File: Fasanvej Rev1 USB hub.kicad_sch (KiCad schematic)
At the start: 23 parts, among them U12 TUSB2036, U13 TPS2042D, Y2 6.000 MHz

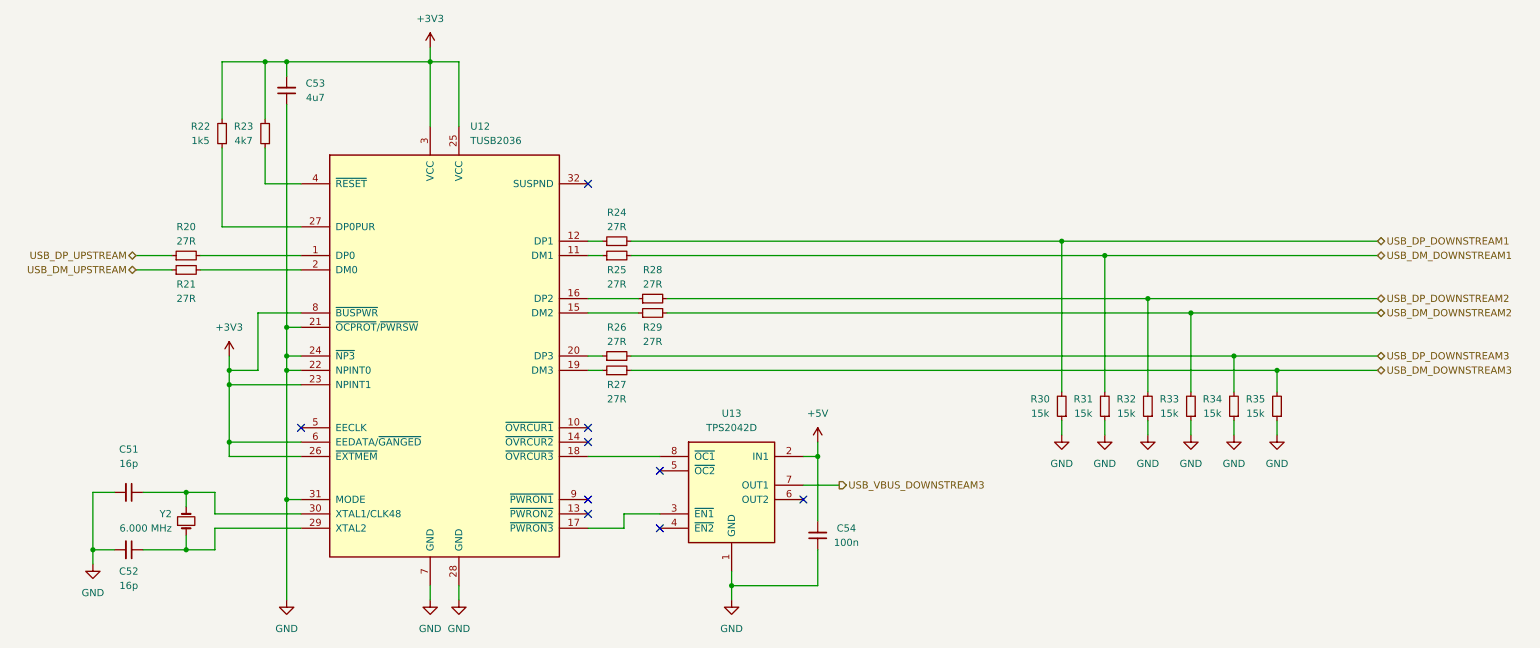
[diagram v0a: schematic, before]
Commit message: Made a lot of progress laying out PCB
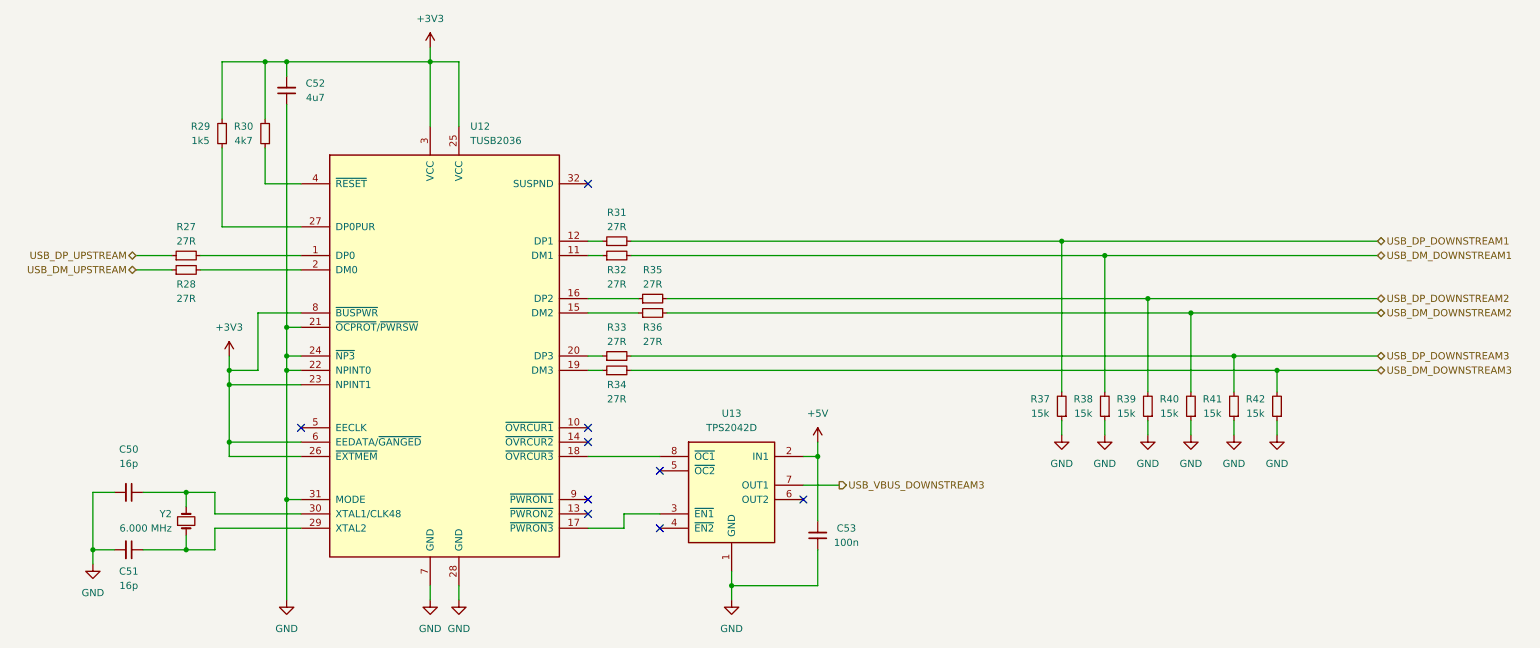
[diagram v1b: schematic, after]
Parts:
- renumbered C51 to C50, C52 to C51, C53 to C52, C54 to C53, R20 to R27, R21 to R28, R22 to R29, R23 to R30, R24 to R31, R25 to R32, R26 to R33, R27 to R34, R28 to R35, R29 to R36, R30 to R37, R31 to R38, R32 to R39, R33 to R40, R34 to R41, R35 to R42
